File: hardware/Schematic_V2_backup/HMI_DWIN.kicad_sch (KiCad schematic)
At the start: 1 part, among them J15 Screw_Terminal_01x04

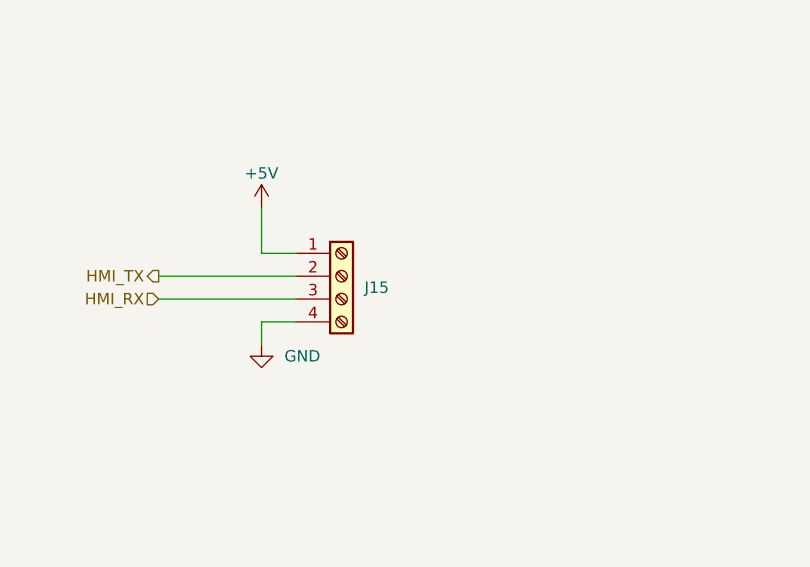
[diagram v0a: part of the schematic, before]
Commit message: Update PCB Layout for Gateway, 23/3/2026
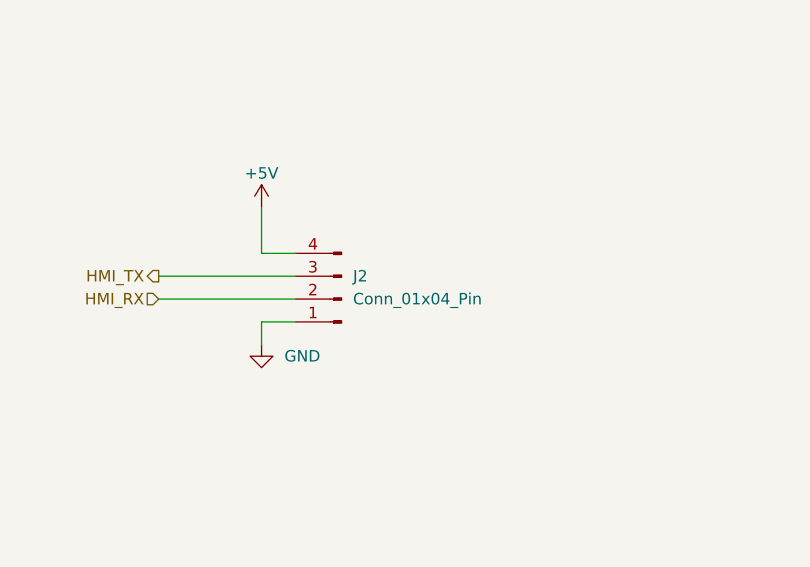
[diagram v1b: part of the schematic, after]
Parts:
- removed J15: Screw_Terminal_01x04, IVS_NEW_FOOTPRINT:Terminal_HT-3.96mm-4P-Horizontal-Pluggable, symbol Connector:Screw_Terminal_01x04
- added J2: Conn_01x04_Pin, IVS_NEW_FOOTPRINT:Conn_XH-P2.54mm-4P, symbol Connector:Conn_01x04_Pin
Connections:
- net +5V: now also J2.4 (Pin_4)
- net GND: now also J2.1 (Pin_1)
- net HMI_RX: now also J2.2 (Pin_2)
- net HMI_TX: now also J2.3 (Pin_3)
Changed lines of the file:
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@@
 	)
 	(symbol
-		(lib_id "Connector:Screw_Terminal_01x04")
-		(at 148.59 90.17 0)
+		(lib_id "Connector:Conn_01x04_Pin")
+		(at 148.59 92.71 180)
 		(unit 1)
 		(exclude_from_sim no)
@@
 		(dnp no)
 		(fields_autoplaced yes)
-		(property "Reference" "J15"
-			(at 151.13 91.4399 0)
+		(property "Reference" "J2"
+			(at 149.86 90.1699 0)
 			(effects
 				(font
 					(size 1.27 1.27)
 				)
-				(justify left)
+				(justify right)
 			)
 		)
-		(property "Value" "Screw_Terminal_01x04"
-			(at 151.13 92.7099 0)
+		(property "Value" "Conn_01x04_Pin"
+			(at 149.86 92.7099 0)
 			(effects
 				(font
 					(size 1.27 1.27)
 				)
-				(justify left)
-				(hide yes)
+				(justify right)
 			)
 		)
-		(property "Footprint" "IVS_NEW_FOOTPRINT:Terminal_HT-3.96mm-4P-Horizontal-Pluggable"
-			(at 148.59 90.17 0)
+		(property "Footprint" "IVS_NEW_FOOTPRINT:Conn_XH-P2.54mm-4P"
+			(at 148.59 92.71 0)
 			(effects
 				(font
@@
 		)
 		(property "Datasheet" "~"
-			(at 148.59 90.17 0)
+			(at 148.59 92.71 0)
 			(effects
 				(font
@@
 			)
 		)
-		(property "Description" "Generic screw terminal, single row, 01x04, script generated (kicad-library-utils/schlib/autogen/connector/)"
-			(at 148.59 90.17 0)
+		(property "Description" "Generic connector, single row, 01x04, script generated"
+			(at 148.59 92.71 0)
 			(effects
 				(font
@@
 			)
 		)
+		(pin "2"
+		)
+		(pin "3"
+		)
 		(pin "4"
-		)
-		(pin "2"
 		)
 		(pin "1"
 		)
-		(pin "3"
-		)
 		(instances
-			(project "DATN_SCHEMATIC"
+			(project ""
 				(path "/08b065f5-231d-43cb-bb9e-87dca43beac9/b068e736-77a3-4da7-b7df-319407e96c28"
-					(reference "J15")
+					(reference "J2")
 					(unit 1)
 				)
